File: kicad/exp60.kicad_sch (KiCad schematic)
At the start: 152 parts, among them K0 KEYSW, K1 KEYSW, K10 KEYSW, K11 KEYSW, K12 KEYSW, K13 KEYSW, K14 KEYSW, K15 KEYSW, K16 KEYSW, K17 KEYSW, K18 KEYSW, K19 KEYSW, K2 KEYSW, K20 KEYSW, K21 KEYSW, K22 KEYSW, K23 KEYSW, K24 KEYSW, K25 KEYSW, K26 KEYSW, K27 KEYSW, K28 KEYSW, K29 KEYSW, K3 KEYSW, K30 KEYSW, K31 KEYSW, K32 KEYSW, K33 KEYSW, K34 KEYSW, K35 KEYSW, K36 KEYSW, K37 KEYSW, K38 KEYSW, K39 KEYSW, K4 KEYSW, K40 KEYSW, K41 KEYSW, K42 KEYSW, K43 KEYSW, K44 KEYSW, K45 KEYSW, K46 KEYSW, K47 KEYSW, K48 KEYSW, K49 KEYSW, K5 KEYSW, K50 KEYSW, K51 KEYSW, K52 KEYSW, K53 KEYSW, K54 KEYSW, K55 KEYSW, K56 KEYSW, K57 KEYSW, K58 KEYSW, K59 KEYSW, K6 KEYSW, K60 KEYSW, K61 KEYSW, K62 KEYSW, K63 KEYSW, K64 KEYSW, K7 KEYSW, K8 KEYSW, K9 KEYSW, SW0 Reset, U0 ATmega32U2, U1 PRTR5V0U2X, Y0 16MHz

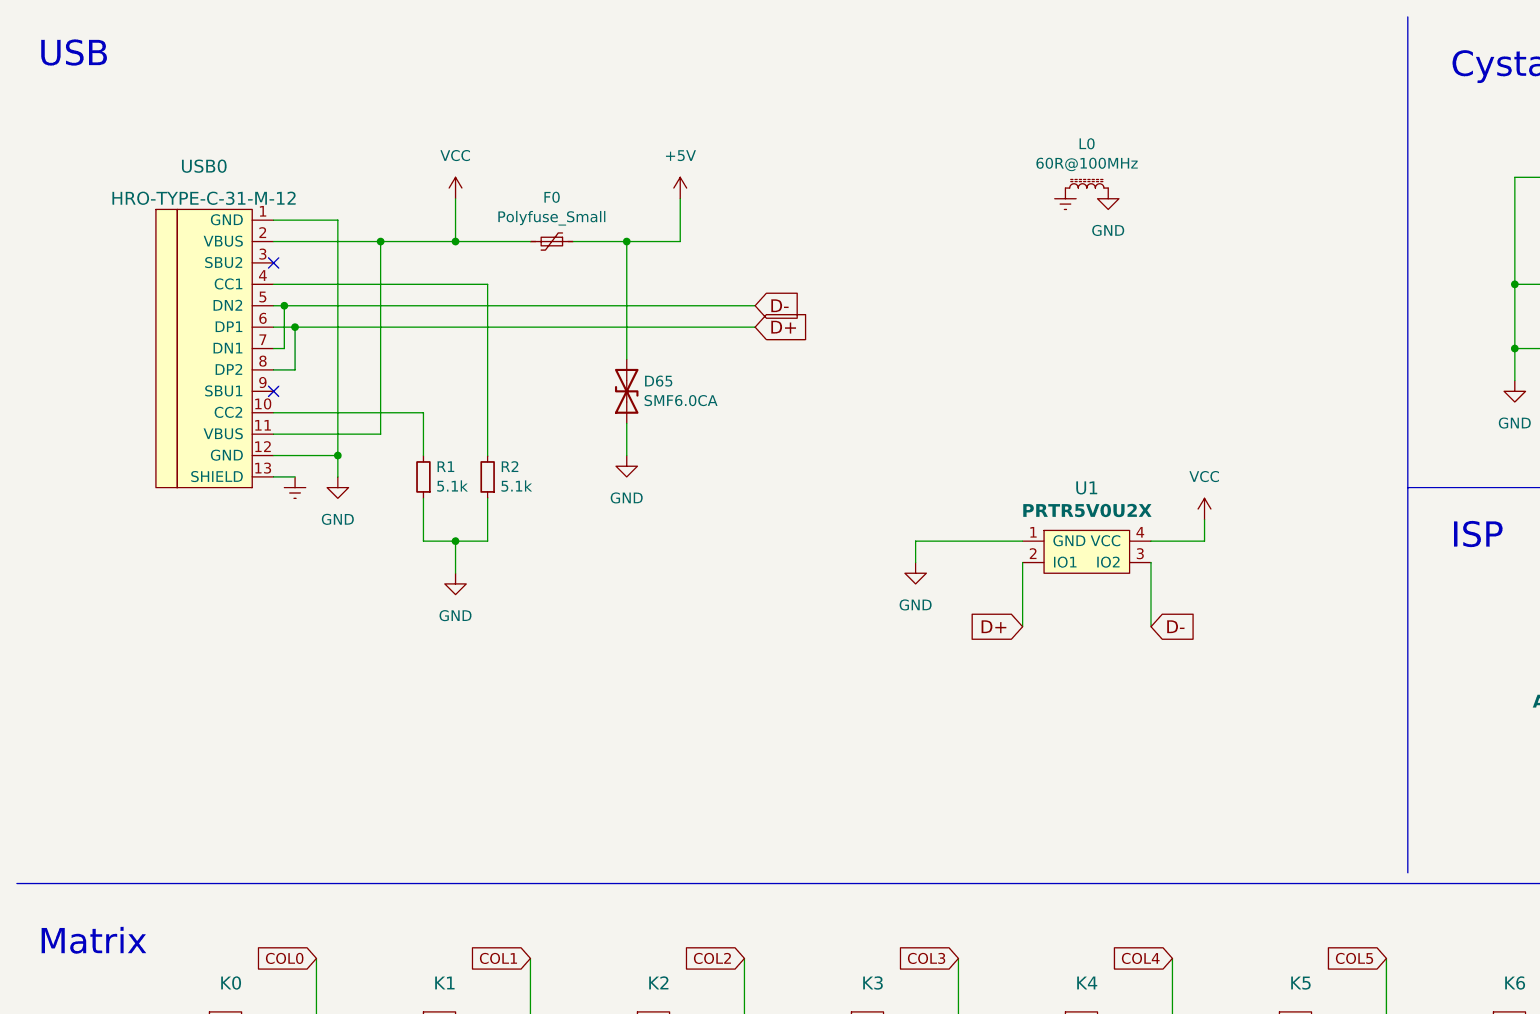
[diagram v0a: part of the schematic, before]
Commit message: replace usb receptacle
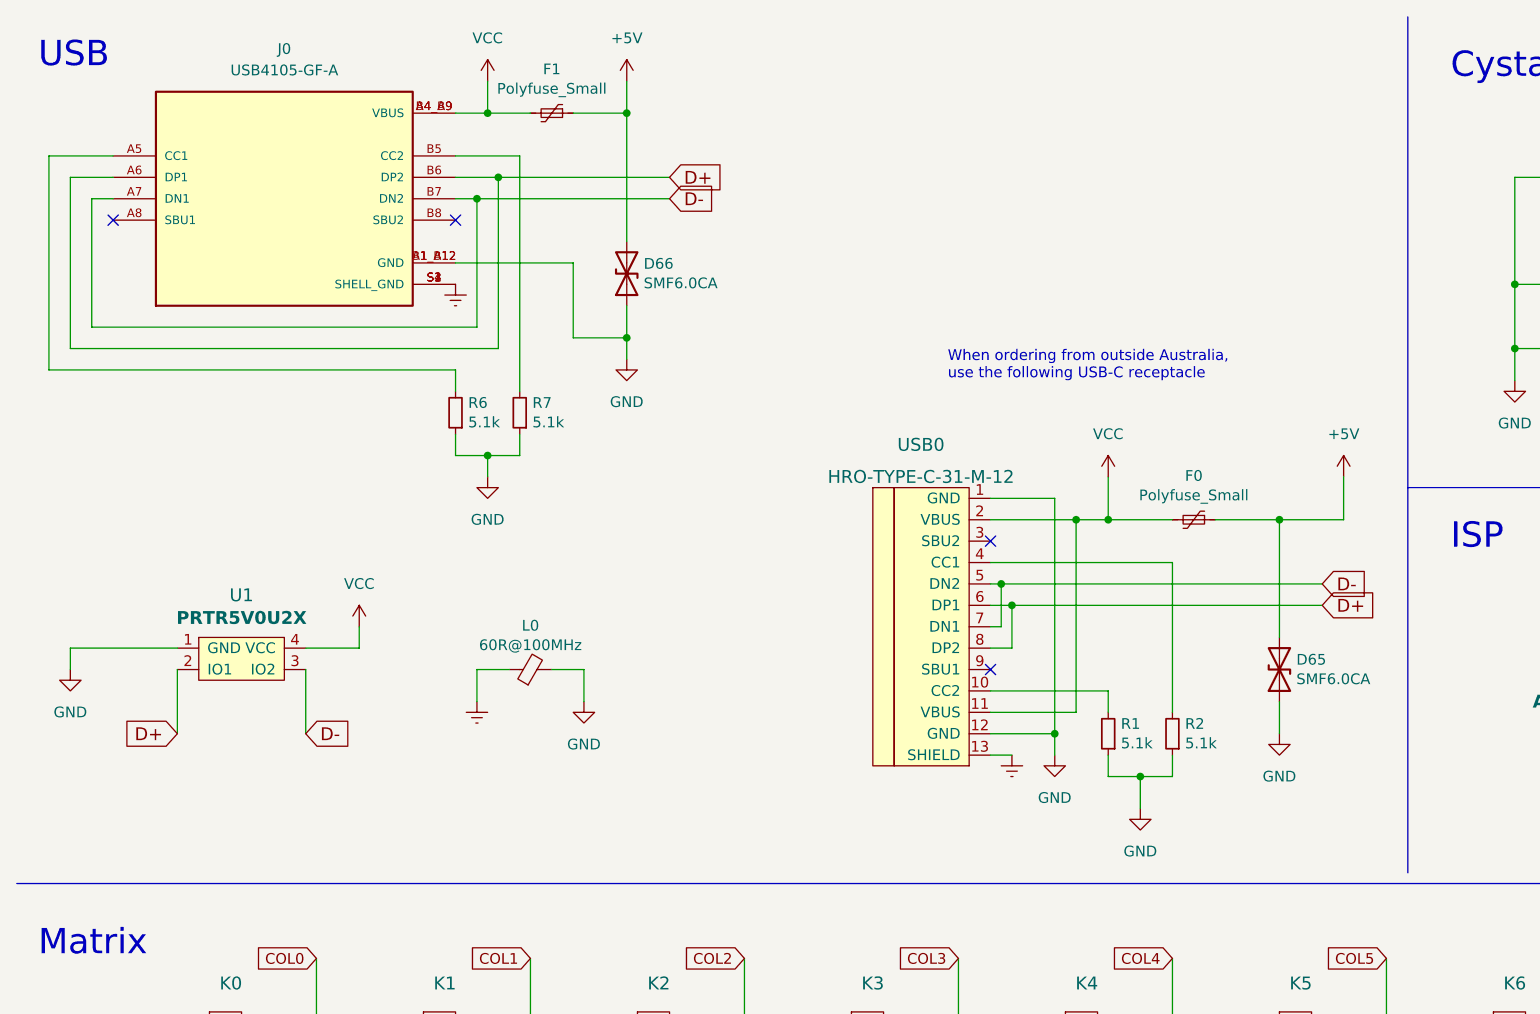
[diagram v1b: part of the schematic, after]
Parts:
- added D66: SMF6.0CA, Diode_SMD:D_SOD-123, symbol Device:D_TVS
- added F1: Polyfuse_Small, Fuse:Fuse_1206_3216Metric, symbol Device:Polyfuse_Small
- added J0: USB4105-GF-A, GCT_USB4105-GF-A:GCT_USB4105-GF-A-HandSoldering, symbol USB4105-GF-A:USB4105-GF-A
- added R6, R7: 5.1k, Resistor_SMD:R_0805_2012Metric, symbol Device:R_Small
- D65, F0, R1, R2, USB0: now left out of the parts list
- L0: symbol JP60-rescue:L_Core_Ferrite_Small-Device -> Device:FerriteBead_Small
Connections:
- net +5V: now also D66.2 (A2), F1.1
- net D+: now also J0.A6 (DP1), J0.B6 (DP2)
- net D-: now also J0.A7 (DN1), J0.B7 (DN2)
- net Earth: now also J0.S1 (SHELL_GND), J0.S2 (SHELL_GND), J0.S3 (SHELL_GND), J0.S4 (SHELL_GND)
- net GND: now also D66.1 (A1), J0.A1_B12 (GND), J0.B1_A12 (GND), R6.1, R7.1
- net VCC: now also F1.2, J0.A4_B9 (VBUS), J0.B4_A9 (VBUS)
- new net: J0.A5 (CC1), R6.2
- new net: J0.B5 (CC2), R7.2
- no-connect marks 2 -> 4
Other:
- note added: "When ordering from outside Australia, use the following USB-C receptacle"
- moved on the sheet: D65, F0, R1, R2, U1, USB0

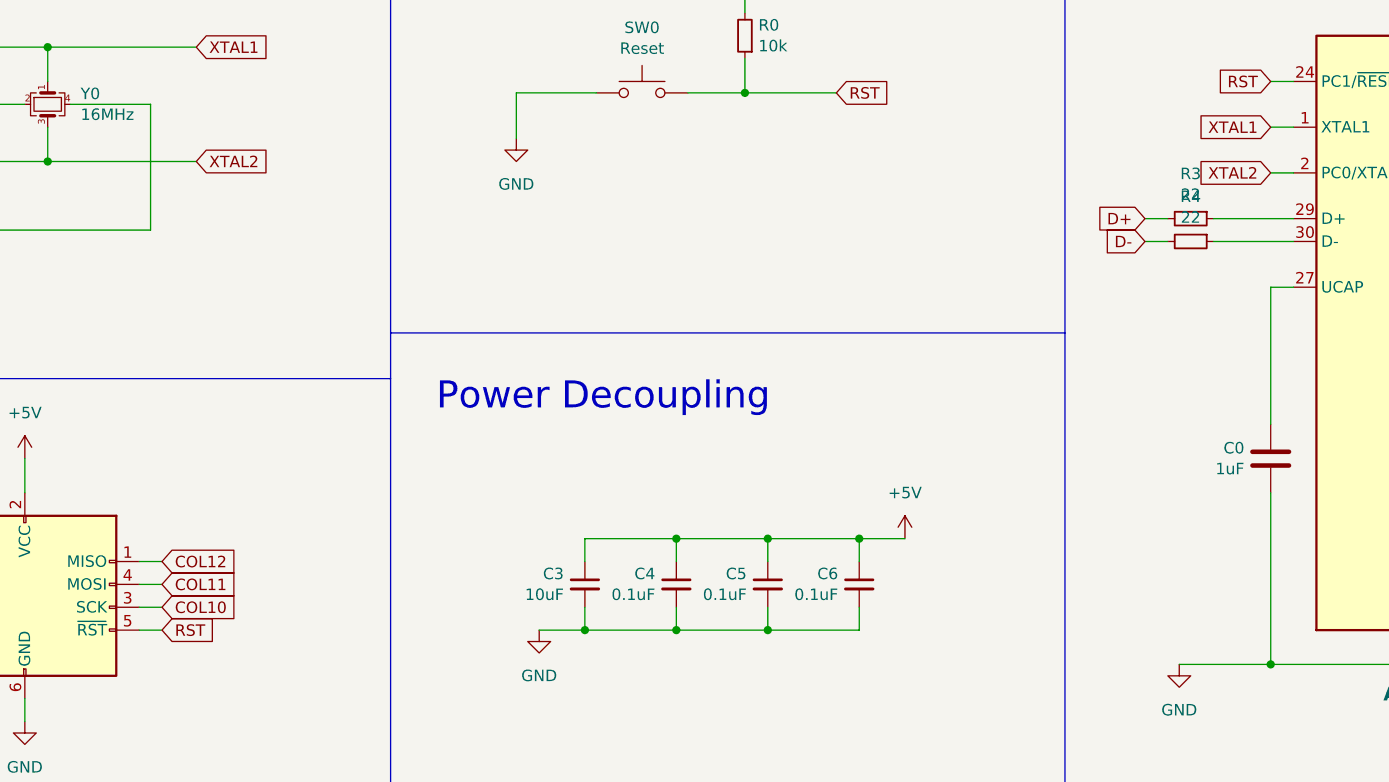
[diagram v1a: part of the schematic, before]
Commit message: fix ISP pins, curved corners, larger component spacing
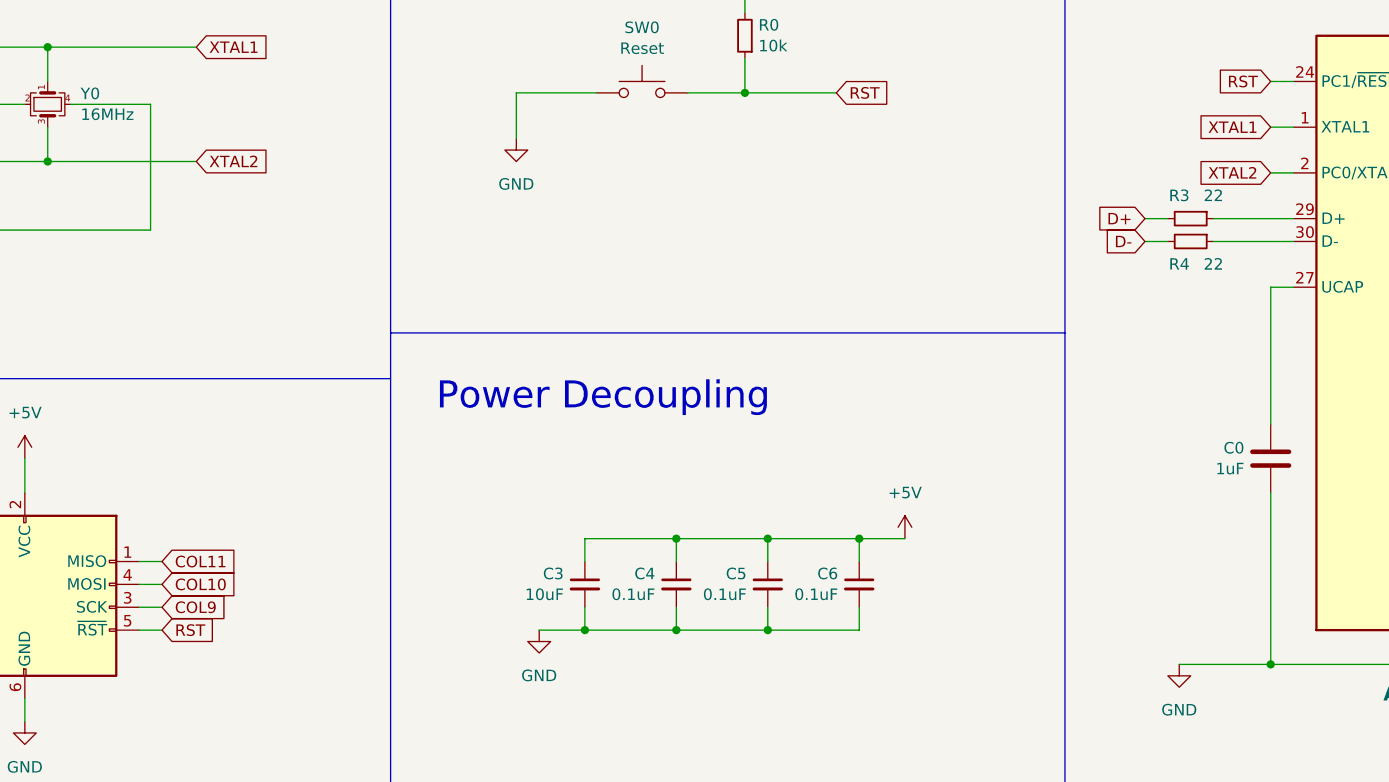
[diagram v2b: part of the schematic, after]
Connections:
- net COL10: now also ISP0.4 (MOSI); no longer ISP0.3 (SCK)
- net COL11: now also ISP0.1 (MISO); no longer ISP0.4 (MOSI)
- net COL12: no longer ISP0.1 (MISO)
- net COL9: now also ISP0.3 (SCK)
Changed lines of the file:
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@@
   (title_block
     (title "Exp60")
-    (rev "1.0")
+    (date "2023-01-19")
+    (rev "1.1")
   )
   (junction (at 316.23 219.71) (diameter 0) (color 0 0 0 0)
@@
     (effects (font (size 3 3)) (justify left bottom))
   )
-  (global_label "COL11" (shape input) (at 226.06 91.44 0) (fields_autoplaced)
+  (global_label "COL10" (shape input) (at 226.06 91.44 0) (fields_autoplaced)
     (effects (font (size 1.27 1.27)) (justify left))
-    (property "Intersheet References" "${INTERSHEET_REFS}" (id 0) (at 234.4318 91.5194 0)
+    (property "Intersheet References" "${INTERSHEET_REFS}" (id 0) (at 234.4318 91.3606 0)
       (effects (font (size 1.27 1.27)) (justify left) hide)
     )
@@
     )
   )
-  (global_label "COL10" (shape input) (at 226.06 93.98 0) (fields_autoplaced)
+  (global_label "COL9" (shape input) (at 226.06 93.98 0) (fields_autoplaced)
     (effects (font (size 1.27 1.27)) (justify left))
-    (property "Intersheet References" "${INTERSHEET_REFS}" (id 0) (at 234.4318 94.0594 0)
+    (property "Intersheet References" "${INTERSHEET_REFS}" (id 0) (at 233.2223 93.9006 0)
       (effects (font (size 1.27 1.27)) (justify left) hide)
     )
@@
     )
   )
-  (global_label "COL12" (shape input) (at 226.06 88.9 0) (fields_autoplaced)
+  (global_label "COL11" (shape input) (at 226.06 88.9 0) (fields_autoplaced)
     (effects (font (size 1.27 1.27)) (justify left))
     (property "Intersheet References" "${INTERSHEET_REFS}" (id 0) (at 234.4318 88.8206 0)
@@
   (symbol (lib_id "Device:R_Small") (at 340.36 50.8 270) (unit 1)
     (in_bom yes) (on_board yes)
-    (property "Reference" "R3" (id 0) (at 340.36 45.8216 90))
-    (property "Value" "22" (id 1) (at 340.36 48.133 90))
+    (property "Reference" "R3" (id 0) (at 339.09 48.26 90))
+    (property "Value" "22" (id 1) (at 342.9 48.26 90))
     (property "Footprint" "Resistor_SMD:R_0805_2012Metric" (id 2) (at 340.36 50.8 0)
       (effects (font (size 1.27 1.27)) hide)
@@
   (symbol (lib_id "Device:R_Small") (at 340.36 53.34 270) (unit 1)
     (in_bom yes) (on_board yes)
-    (property "Reference" "R4" (id 0) (at 340.36 48.3616 90))
-    (property "Value" "22" (id 1) (at 340.36 50.673 90))
+    (property "Reference" "R4" (id 0) (at 339.09 55.88 90))
+    (property "Value" "22" (id 1) (at 342.9 55.88 90))
     (property "Footprint" "Resistor_SMD:R_0805_2012Metric" (id 2) (at 340.36 53.34 0)
       (effects (font (size 1.27 1.27)) hide)
